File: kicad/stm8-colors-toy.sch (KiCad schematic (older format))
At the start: 14 parts

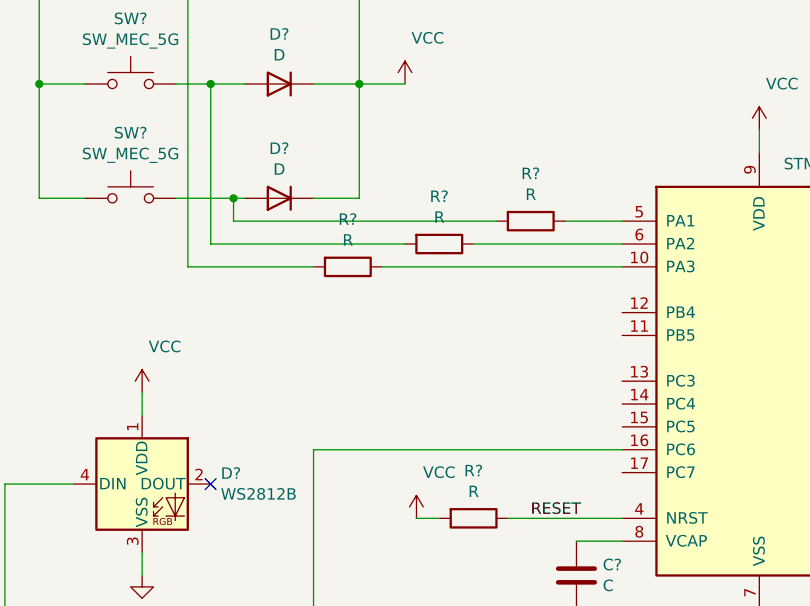
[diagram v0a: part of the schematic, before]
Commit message: Add pulldowns for buttons
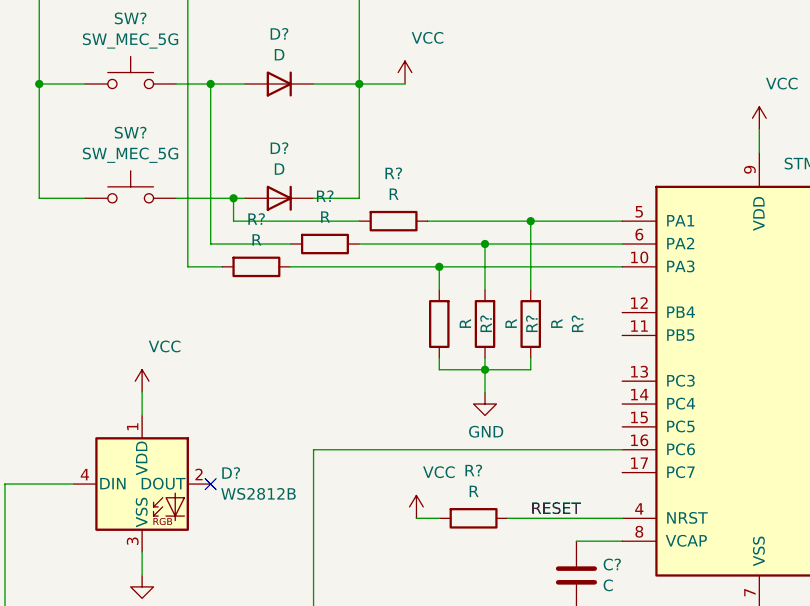
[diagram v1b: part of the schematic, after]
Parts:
- added R? (x3): R, symbol Device:R
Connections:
- wire segments 48 -> 60
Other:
- moved on the sheet: R?
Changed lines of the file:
@@
 L Device:R R?
 U 1 1 5FF37449
-P 3550 2100
-F 0 "R?" V 3343 2100 50  0000 C CNN
-F 1 "R" V 3434 2100 50  0000 C CNN
-F 2 "" V 3480 2100 50  0001 C CNN
-F 3 "~" H 3550 2100 50  0001 C CNN
-	1    3550 2100
+P 2950 2100
+F 0 "R?" V 2743 2100 50  0000 C CNN
+F 1 "R" V 2834 2100 50  0000 C CNN
+F 2 "" V 2880 2100 50  0001 C CNN
+F 3 "~" H 2950 2100 50  0001 C CNN
+	1    2950 2100
 	0    1    1    0
 $EndComp
@@
 L Device:R R?
 U 1 1 5FF37A5C
-P 3150 2200
-F 0 "R?" V 2943 2200 50  0000 C CNN
-F 1 "R" V 3034 2200 50  0000 C CNN
-F 2 "" V 3080 2200 50  0001 C CNN
-F 3 "~" H 3150 2200 50  0001 C CNN
-	1    3150 2200
+P 2650 2200
+F 0 "R?" V 2443 2200 50  0000 C CNN
+F 1 "R" V 2534 2200 50  0000 C CNN
+F 2 "" V 2580 2200 50  0001 C CNN
+F 3 "~" H 2650 2200 50  0001 C CNN
+	1    2650 2200
 	0    1    1    0
 $EndComp
@@
 L Device:R R?
 U 1 1 5FF37F7A
-P 2750 2300
-F 0 "R?" V 2543 2300 50  0000 C CNN
-F 1 "R" V 2634 2300 50  0000 C CNN
-F 2 "" V 2680 2300 50  0001 C CNN
-F 3 "~" H 2750 2300 50  0001 C CNN
-	1    2750 2300
-	0    1    1    0
-$EndComp
-Wire Wire Line
-	2250 2100 3400 2100
-Wire Wire Line
-	2150 2200 3000 2200
-Wire Wire Line
-	2050 2300 2600 2300
-Wire Wire Line
-	2900 2300 3950 2300
-Wire Wire Line
-	3300 2200 3950 2200
-Wire Wire Line
-	3700 2100 3950 2100
+P 2350 2300
+F 0 "R?" V 2143 2300 50  0000 C CNN
+F 1 "R" V 2234 2300 50  0000 C CNN
+F 2 "" V 2280 2300 50  0001 C CNN
+F 3 "~" H 2350 2300 50  0001 C CNN
+	1    2350 2300
+	0    1    1    0
+$EndComp
+Wire Wire Line
+	2250 2100 2800 2100
+Wire Wire Line
+	2150 2200 2500 2200
+Wire Wire Line
+	2050 2300 2200 2300
+Wire Wire Line
+	2500 2300 3150 2300
+Wire Wire Line
+	3100 2100 3550 2100
 $Comp
 L LED:WS2812B D?
@@
 Text Label 5200 2900 0    50   ~ 0
 UART_TX
+$Comp
+L Device:R R?
+U 1 1 5FF48C5F
+P 3550 2550
+F 0 "R?" V 3343 2550 50  0000 C CNN
+F 1 "R" V 3434 2550 50  0000 C CNN
+F 2 "" V 3480 2550 50  0001 C CNN
+F 3 "~" H 3550 2550 50  0001 C CNN
+	1    3550 2550
+	-1   0    0    1
+$EndComp
+$Comp
+L Device:R R?
+U 1 1 5FF4B913
+P 3350 2550
+F 0 "R?" V 3143 2550 50  0000 C CNN
+F 1 "R" V 3234 2550 50  0000 C CNN
+F 2 "" V 3280 2550 50  0001 C CNN
+F 3 "~" H 3350 2550 50  0001 C CNN
+	1    3350 2550
+	-1   0    0    1
+$EndComp
+$Comp
+L Device:R R?
+U 1 1 5FF4BF60
+P 3150 2550
+F 0 "R?" V 2943 2550 50  0000 C CNN
+F 1 "R" V 3034 2550 50  0000 C CNN
+F 2 "" V 3080 2550 50  0001 C CNN
+F 3 "~" H 3150 2550 50  0001 C CNN
+	1    3150 2550
+	-1   0    0    1
+$EndComp
+Wire Wire Line
+	3550 2100 3550 2400
+Connection ~ 3550 2100
+Wire Wire Line
+	3550 2100 3950 2100
+Wire Wire Line
+	3350 2200 3350 2400
+Connection ~ 3350 2200
+Wire Wire Line
+	3350 2200 3950 2200
+Wire Wire Line
+	3550 2700 3550 2750
+Wire Wire Line
+	3550 2750 3350 2750
+Wire Wire Line
+	3350 2700 3350 2750
+Connection ~ 3350 2750
+Wire Wire Line
+	3350 2750 3150 2750
+$Comp
+L power:GND #PWR?
+U 1 1 5FF50513
+P 3350 2850
+F 0 "#PWR?" H 3350 2600 50  0001 C CNN
+F 1 "GND" H 3355 2677 50  0000 C CNN
+F 2 "" H 3350 2850 50  0001 C CNN
+F 3 "" H 3350 2850 50  0001 C CNN
+	1    3350 2850
+	1    0    0    -1
+$EndComp
+Wire Wire Line
+	3150 2700 3150 2750
+Wire Wire Line
+	2800 2200 3350 2200
+Connection ~ 3150 2300
+Wire Wire Line
+	3150 2300 3950 2300
+Wire Wire Line
+	3150 2300 3150 2400
+Wire Wire Line
+	3350 2750 3350 2850
 $EndSCHEMATC
